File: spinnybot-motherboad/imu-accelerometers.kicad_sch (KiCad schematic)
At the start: 19 parts, among them U10 MMA3221KEG, U11 ADS122U04IPWR, U12 ADS122U04IPWR, U4 ICM-20649, U6 74LVC1G157GV_125, U8 SN74LVC1G18DBVR, U9 MMA3221KEG

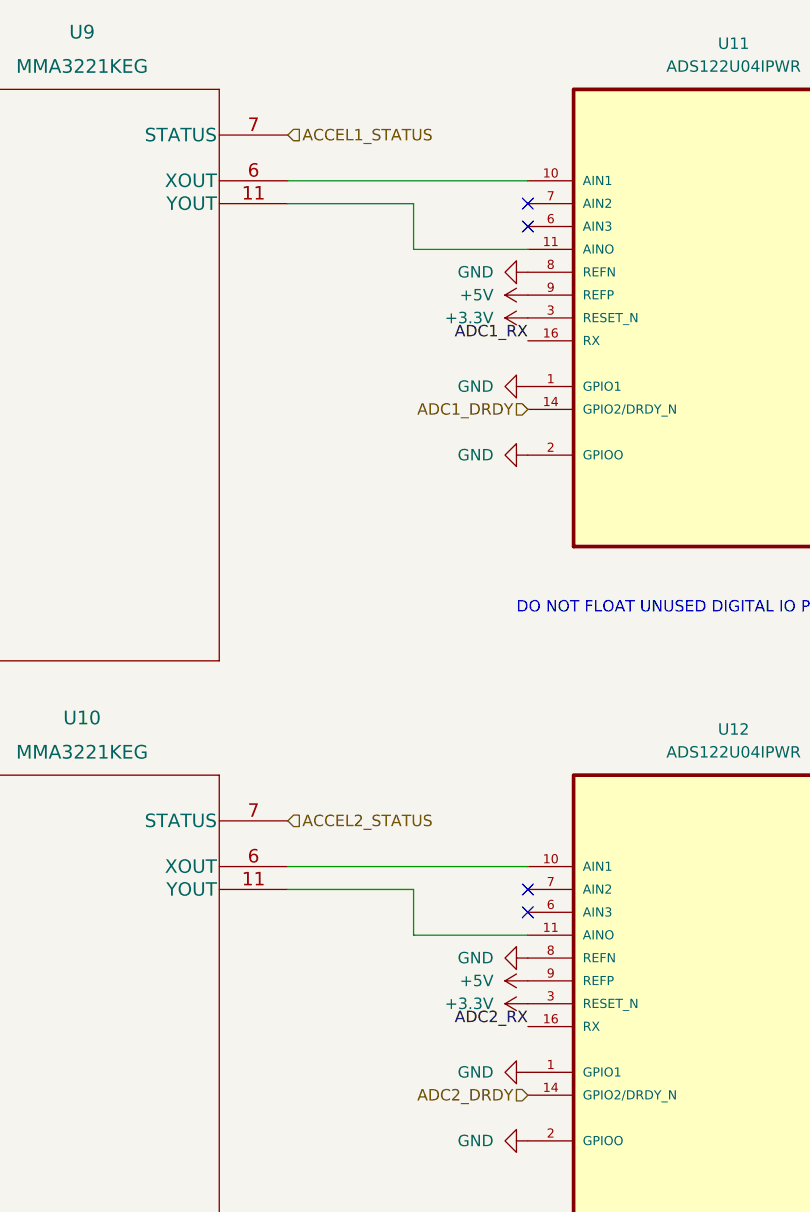
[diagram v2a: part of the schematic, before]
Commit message: Addressed Pratik's concerns about cap placement and missing caps
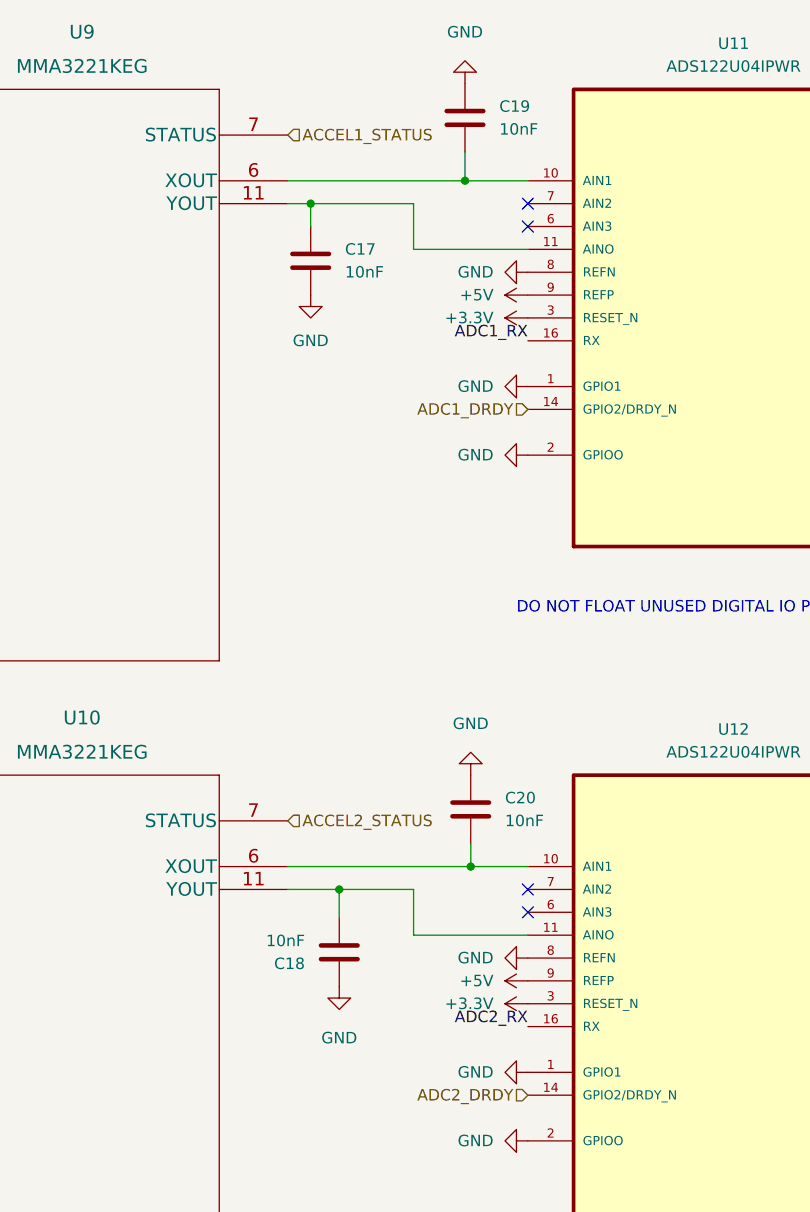
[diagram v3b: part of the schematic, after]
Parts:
- added C17, C18, C19, C20: 10nF, Capacitor_SMD:C_0805_2012Metric_Pad1.18x1.45mm_HandSolder, symbol Device:C
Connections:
- net GND: now also C17.2, C18.1, C19.1, C20.1
- net at U10.11 (YOUT), U12.11 (AINO): now also C18.2
- net at U10.6 (XOUT), U12.10 (AIN1): now also C20.2
- net at U11.11 (AINO), U9.11 (YOUT): now also C17.1
- net at U11.10 (AIN1), U9.6 (XOUT): now also C19.2
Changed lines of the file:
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@@
   (junction (at 81.28 68.58) (diameter 1.016) (color 0 0 0 0)
   )
+  (junction (at 191.135 36.83) (diameter 0) (color 0 0 0 0)
+  )
   (junction (at 81.28 62.23) (diameter 1.016) (color 0 0 0 0)
   )
@@
   (junction (at 251.46 57.15) (diameter 0) (color 0 0 0 0)
   )
+  (junction (at 191.77 113.03) (diameter 0) (color 0 0 0 0)
+  )
   (junction (at 123.19 85.09) (diameter 0) (color 0 0 0 0)
   )
+  (junction (at 177.165 115.57) (diameter 0) (color 0 0 0 0)
+  )
   (junction (at 123.19 77.47) (diameter 0) (color 0 0 0 0)
+  )
+  (junction (at 173.99 39.37) (diameter 0) (color 0 0 0 0)
   )
   (junction (at 247.65 151.13) (diameter 0) (color 0 0 0 0)
@@
     (stroke (width 0) (type default) (color 0 0 0 0))
   )
+  (wire (pts (xy 191.135 36.83) (xy 198.12 36.83))
+    (stroke (width 0) (type default) (color 0 0 0 0))
+  )
+  (wire (pts (xy 173.99 39.37) (xy 173.99 41.91))
+    (stroke (width 0) (type default) (color 0 0 0 0))
+  )
   (wire (pts (xy 125.73 151.13) (xy 123.19 151.13))
     (stroke (width 0) (type default) (color 0 0 0 0))
@@
     (stroke (width 0) (type default) (color 0 0 0 0))
   )
+  (wire (pts (xy 191.135 33.655) (xy 191.135 36.83))
+    (stroke (width 0) (type default) (color 0 0 0 0))
+  )
   (wire (pts (xy 251.46 57.15) (xy 256.54 57.15))
     (stroke (width 0) (type default) (color 0 0 0 0))
@@
     (stroke (width 0) (type default) (color 0 0 0 0))
   )
-  (wire (pts (xy 171.45 115.57) (xy 185.42 115.57))
+  (wire (pts (xy 171.45 115.57) (xy 177.165 115.57))
     (stroke (width 0) (type default) (color 0 0 0 0))
   )
@@
     (stroke (width 0) (type solid) (color 0 0 0 0))
   )
-  (wire (pts (xy 171.45 36.83) (xy 198.12 36.83))
+  (wire (pts (xy 171.45 36.83) (xy 191.135 36.83))
     (stroke (width 0) (type default) (color 0 0 0 0))
   )
@@
     (stroke (width 0) (type default) (color 0 0 0 0))
   )
+  (wire (pts (xy 191.77 110.49) (xy 191.77 113.03))
+    (stroke (width 0) (type default) (color 0 0 0 0))
+  )
   (wire (pts (xy 116.84 143.51) (xy 116.84 153.67))
     (stroke (width 0) (type default) (color 0 0 0 0))
@@
     (stroke (width 0) (type default) (color 0 0 0 0))
   )
+  (wire (pts (xy 177.165 118.745) (xy 177.165 115.57))
+    (stroke (width 0) (type default) (color 0 0 0 0))
+  )
   (wire (pts (xy 246.38 105.41) (xy 243.84 105.41))
     (stroke (width 0) (type default) (color 0 0 0 0))
@@
     (stroke (width 0) (type default) (color 0 0 0 0))
   )
-  (wire (pts (xy 171.45 113.03) (xy 198.12 113.03))
+  (wire (pts (xy 171.45 113.03) (xy 191.77 113.03))
     (stroke (width 0) (type default) (color 0 0 0 0))
   )
@@
     (stroke (width 0) (type default) (color 0 0 0 0))
   )
+  (wire (pts (xy 191.77 113.03) (xy 198.12 113.03))
+    (stroke (width 0) (type default) (color 0 0 0 0))
+  )
   (wire (pts (xy 185.42 120.65) (xy 198.12 120.65))
     (stroke (width 0) (type default) (color 0 0 0 0))
@@
     (stroke (width 0) (type solid) (color 0 0 0 0))
   )
-  (wire (pts (xy 171.45 39.37) (xy 185.42 39.37))
+  (wire (pts (xy 173.99 39.37) (xy 185.42 39.37))
+    (stroke (width 0) (type default) (color 0 0 0 0))
+  )
+  (wire (pts (xy 171.45 39.37) (xy 173.99 39.37))
     (stroke (width 0) (type default) (color 0 0 0 0))
   )
@@
   )
   (wire (pts (xy 123.19 85.09) (xy 125.73 85.09))
+    (stroke (width 0) (type default) (color 0 0 0 0))
+  )
+  (wire (pts (xy 177.165 115.57) (xy 185.42 115.57))
     (stroke (width 0) (type default) (color 0 0 0 0))
   )
@@
     (pin "2")
   )
+  (symbol (lib_id "Device:C") (at 191.135 29.845 0) (unit 1)
+    (in_bom yes) (on_board yes) (fields_autoplaced)
+    (property "Reference" "C19" (id 0) (at 194.945 28.5749 0)
+      (effects (font (size 1.27 1.27)) (justify left))
+    )
+    (property "Value" "10nF" (id 1) (at 194.945 31.1149 0)
+      (effects (font (size 1.27 1.27)) (justify left))
+    )
+    (property "Footprint" "Capacitor_SMD:C_0805_2012Metric_Pad1.18x1.45mm_HandSolder" (id 2) (at 192.1002 33.655 0)
+      (effects (font (size 1.27 1.27)) hide)
+    )
+    (property "Datasheet" "~" (id 3) (at 191.135 29.845 0)
+      (effects (font (size 1.27 1.27)) hide)
+    )
+    (pin "1")
+    (pin "2")
+  )
   (symbol (lib_id "power:+5V") (at 246.38 125.73 0) (unit 1)
     (in_bom yes) (on_board yes) (fields_autoplaced)
@@
     (pin "1")
   )
+  (symbol (lib_id "Device:C") (at 173.99 45.72 0) (unit 1)
+    (in_bom yes) (on_board yes) (fields_autoplaced)
+    (property "Reference" "C17" (id 0) (at 177.8 44.4499 0)
+      (effects (font (size 1.27 1.27)) (justify left))
+    )
+    (property "Value" "10nF" (id 1) (at 177.8 46.9899 0)
+      (effects (font (size 1.27 1.27)) (justify left))
+    )
+    (property "Footprint" "Capacitor_SMD:C_0805_2012Metric_Pad1.18x1.45mm_HandSolder" (id 2) (at 174.9552 49.53 0)
+      (effects (font (size 1.27 1.27)) hide)
+    )
+    (property "Datasheet" "~" (id 3) (at 173.99 45.72 0)
+      (effects (font (size 1.27 1.27)) hide)
+    )
+    (pin "1")
+    (pin "2")
+  )
+  (symbol (lib_id "Device:C") (at 191.77 106.68 0) (unit 1)
+    (in_bom yes) (on_board yes) (fields_autoplaced)
+    (property "Reference" "C20" (id 0) (at 195.58 105.4099 0)
+      (effects (font (size 1.27 1.27)) (justify left))
+    )
+    (property "Value" "10nF" (id 1) (at 195.58 107.9499 0)
+      (effects (font (size 1.27 1.27)) (justify left))
+    )
+    (property "Footprint" "Capacitor_SMD:C_0805_2012Metric_Pad1.18x1.45mm_HandSolder" (id 2) (at 192.7352 110.49 0)
+      (effects (font (size 1.27 1.27)) hide)
+    )
+    (property "Datasheet" "~" (id 3) (at 191.77 106.68 0)
+      (effects (font (size 1.27 1.27)) hide)
+    )
+    (pin "1")
+    (pin "2")
+  )
   (symbol (lib_id "power:GND") (at 21.59 154.94 0) (unit 1)
     (in_bom yes) (on_board yes) (fields_autoplaced)
@@
     )
     (property "Datasheet" "" (id 3) (at 116.84 91.44 0)
+      (effects (font (size 1.27 1.27)) hide)
+    )
+    (pin "1")
+  )
+  (symbol (lib_id "power:GND") (at 173.99 49.53 0) (unit 1)
+    (in_bom yes) (on_board yes) (fields_autoplaced)
+    (property "Reference" "#PWR0163" (id 0) (at 173.99 55.88 0)
+      (effects (font (size 1.27 1.27)) hide)
+    )
+    (property "Value" "GND" (id 1) (at 173.99 54.61 0))
+    (property "Footprint" "" (id 2) (at 173.99 49.53 0)
+      (effects (font (size 1.27 1.27)) hide)
+    )
+    (property "Datasheet" "" (id 3) (at 173.99 49.53 0)
       (effects (font (size 1.27 1.27)) hide)
     )
@@
     (pin "6")
   )
+  (symbol (lib_id "Device:C") (at 177.165 122.555 180) (unit 1)
+    (in_bom yes) (on_board yes) (fields_autoplaced)
+    (property "Reference" "C18" (id 0) (at 173.355 123.8251 0)
+      (effects (font (size 1.27 1.27)) (justify left))
+    )
+    (property "Value" "10nF" (id 1) (at 173.355 121.2851 0)
+      (effects (font (size 1.27 1.27)) (justify left))
+    )
+    (property "Footprint" "Capacitor_SMD:C_0805_2012Metric_Pad1.18x1.45mm_HandSolder" (id 2) (at 176.1998 118.745 0)
+      (effects (font (size 1.27 1.27)) hide)
+    )
+    (property "Datasheet" "~" (id 3) (at 177.165 122.555 0)
+      (effects (font (size 1.27 1.27)) hide)
+    )
+    (pin "1")
+    (pin "2")
+  )
+  (symbol (lib_id "power:GND") (at 177.165 126.365 0) (unit 1)
+    (in_bom yes) (on_board yes) (fields_autoplaced)
+    (property "Reference" "#PWR0165" (id 0) (at 177.165 132.715 0)
+      (effects (font (size 1.27 1.27)) hide)
+    )
+    (property "Value" "GND" (id 1) (at 177.165 132.08 0))
+    (property "Footprint" "" (id 2) (at 177.165 126.365 0)
+      (effects (font (size 1.27 1.27)) hide)
+    )
+    (property "Datasheet" "" (id 3) (at 177.165 126.365 0)
+      (effects (font (size 1.27 1.27)) hide)
+    )
+    (pin "1")
+  )
   (symbol (lib_id "power:GND") (at 198.12 143.51 270) (unit 1)
     (in_bom yes) (on_board yes) (fields_autoplaced)
@@
     (pin "1")
   )
+  (symbol (lib_id "power:GND") (at 191.135 26.035 180) (unit 1)
+    (in_bom yes) (on_board yes) (fields_autoplaced)
+    (property "Reference" "#PWR0162" (id 0) (at 191.135 19.685 0)
+      (effects (font (size 1.27 1.27)) hide)
+    )
+    (property "Value" "GND" (id 1) (at 191.135 20.32 0))
+    (property "Footprint" "" (id 2) (at 191.135 26.035 0)
+      (effects (font (size 1.27 1.27)) hide)
+    )
+    (property "Datasheet" "" (id 3) (at 191.135 26.035 0)
+      (effects (font (size 1.27 1.27)) hide)
+    )
+    (pin "1")
+  )
   (symbol (lib_id "Device:C") (at 256.54 53.34 0) (unit 1)
     (in_bom yes) (on_board yes) (fields_autoplaced)
@@
       (effects (font (size 1.27 1.27)) hide)
     )
+    (pin "1")
+  )
+  (symbol (lib_id "power:GND") (at 191.77 102.87 180) (unit 1)
+    (in_bom yes) (on_board yes) (fields_autoplaced)
+    (property "Reference" "#PWR0164" (id 0) (at 191.77 96.52 0)
+      (effects (font (size 1.27 1.27)) hide)
+    )
+    (property "Value" "GND" (id 1) (at 191.77 97.155 0))
+    (property "Footprint" "" (id 2) (at 191.77 102.87 0)
+      (effects (font (size 1.27 1.27)) hide)
+    )
+    (property "Datasheet" "" (id 3) (at 191.77 102.87 0)
+      (effects (font (size 1.27 1.27)) hide)
+    )
